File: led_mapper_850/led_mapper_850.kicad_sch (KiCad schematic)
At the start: 1082 parts, among them J1 Conn_02x12_Top_Bottom

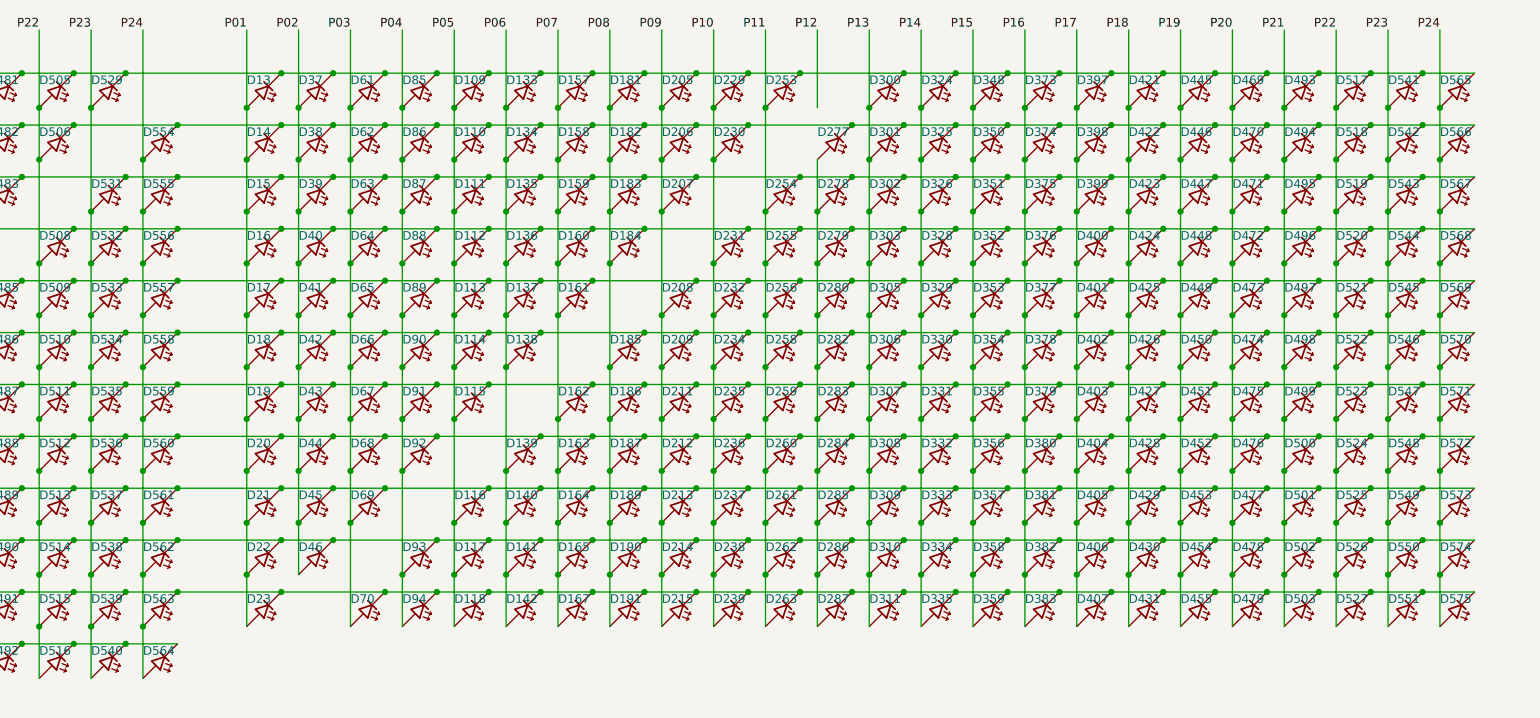
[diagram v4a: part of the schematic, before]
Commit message: fix horizontal connections
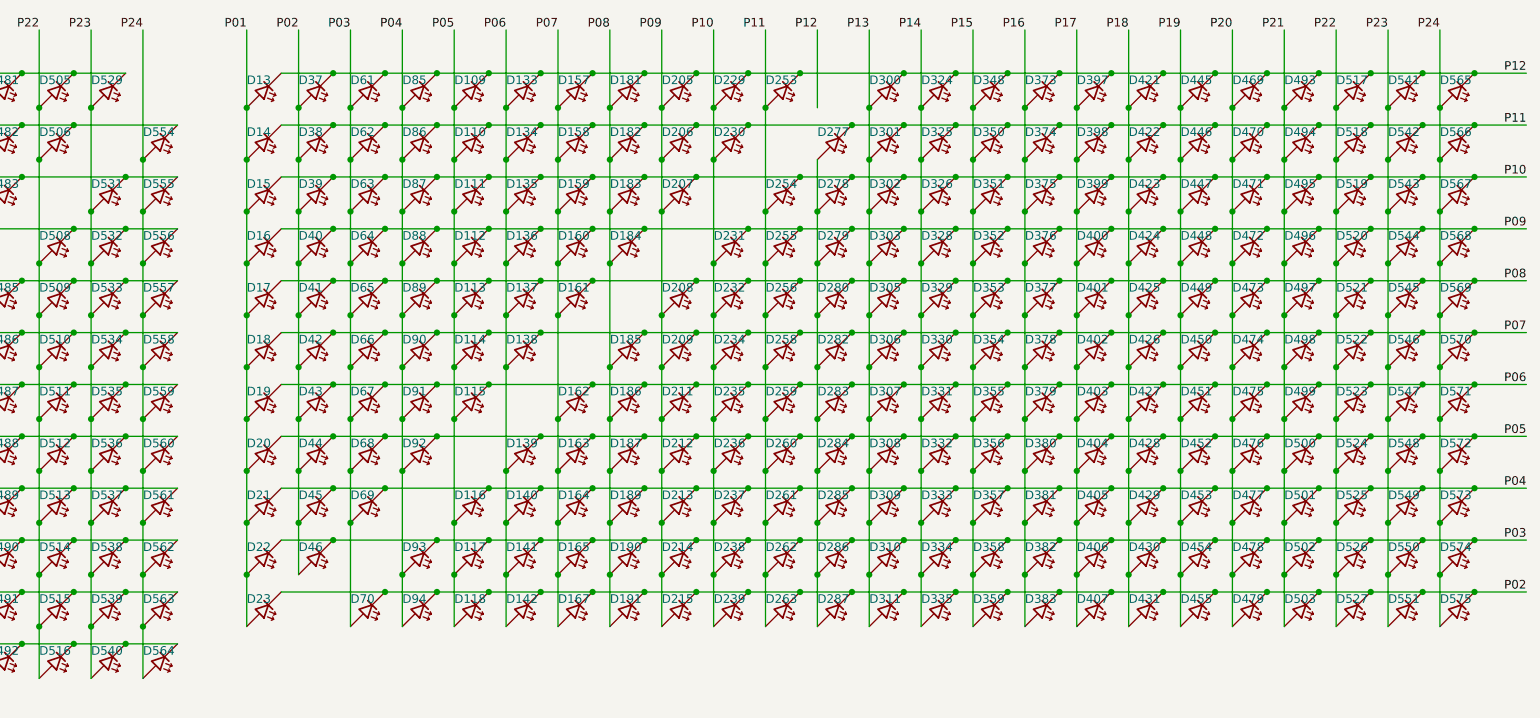
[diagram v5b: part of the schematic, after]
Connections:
- net P02: now also D118.1 (K), D142.1 (K), D167.1 (K), D191.1 (K), D215.1 (K), D23.1 (K), D239.1 (K), D263.1 (K), D287.1 (K), D311.1 (K), D335.1 (K), D359.1 (K), D383.1 (K), D407.1 (K), D431.1 (K), D455.1 (K), D479.1 (K), D503.1 (K), D527.1 (K), D551.1 (K), D575.1 (K), D70.1 (K), D94.1 (K)
- net P03: now also D117.1 (K), D141.1 (K), D165.1 (K), D190.1 (K), D214.1 (K), D22.1 (K), D238.1 (K), D262.1 (K), D286.1 (K), D310.1 (K), D334.1 (K), D358.1 (K), D382.1 (K), D406.1 (K), D430.1 (K), D454.1 (K), D46.1 (K), D478.1 (K), D502.1 (K), D526.1 (K), D550.1 (K), D574.1 (K), D93.1 (K)
- net P04: now also D116.1 (K), D140.1 (K), D164.1 (K), D189.1 (K), D21.1 (K), D213.1 (K), D237.1 (K), D261.1 (K), D285.1 (K), D309.1 (K), D333.1 (K), D357.1 (K), D381.1 (K), D405.1 (K), D429.1 (K), D45.1 (K), D453.1 (K), D477.1 (K), D501.1 (K), D525.1 (K), D549.1 (K), D573.1 (K), D69.1 (K)
- net P05: now also D139.1 (K), D163.1 (K), D187.1 (K), D20.1 (K), D212.1 (K), D236.1 (K), D260.1 (K), D284.1 (K), D308.1 (K), D332.1 (K), D356.1 (K), D380.1 (K), D404.1 (K), D428.1 (K), D44.1 (K), D452.1 (K), D476.1 (K), D500.1 (K), D524.1 (K), D548.1 (K), D572.1 (K), D68.1 (K), D92.1 (K)
- net P06: now also D115.1 (K), D162.1 (K), D186.1 (K), D19.1 (K), D211.1 (K), D235.1 (K), D259.1 (K), D283.1 (K), D307.1 (K), D331.1 (K), D355.1 (K), D379.1 (K), D403.1 (K), D427.1 (K), D43.1 (K), D451.1 (K), D475.1 (K), D499.1 (K), D523.1 (K), D547.1 (K), D571.1 (K), D67.1 (K), D91.1 (K)
- net P07: now also D114.1 (K), D138.1 (K), D18.1 (K), D185.1 (K), D209.1 (K), D234.1 (K), D258.1 (K), D282.1 (K), D306.1 (K), D330.1 (K), D354.1 (K), D378.1 (K), D402.1 (K), D42.1 (K), D426.1 (K), D450.1 (K), D474.1 (K), D498.1 (K), D522.1 (K), D546.1 (K), D570.1 (K), D66.1 (K), D90.1 (K)
- net P08: now also D113.1 (K), D137.1 (K), D161.1 (K), D17.1 (K), D208.1 (K), D232.1 (K), D256.1 (K), D280.1 (K), D305.1 (K), D329.1 (K), D353.1 (K), D377.1 (K), D401.1 (K), D41.1 (K), D425.1 (K), D449.1 (K), D473.1 (K), D497.1 (K), D521.1 (K), D545.1 (K), D569.1 (K), D65.1 (K), D89.1 (K)
- net P09: now also D112.1 (K), D136.1 (K), D16.1 (K), D160.1 (K), D184.1 (K), D231.1 (K), D255.1 (K), D279.1 (K), D303.1 (K), D328.1 (K), D352.1 (K), D376.1 (K), D40.1 (K), D400.1 (K), D424.1 (K), D448.1 (K), D472.1 (K), D496.1 (K), D520.1 (K), D544.1 (K), D568.1 (K), D64.1 (K), D88.1 (K)
- net P10: now also D111.1 (K), D135.1 (K), D15.1 (K), D159.1 (K), D183.1 (K), D207.1 (K), D254.1 (K), D278.1 (K), D302.1 (K), D326.1 (K), D351.1 (K), D375.1 (K), D39.1 (K), D399.1 (K), D423.1 (K), D447.1 (K), D471.1 (K), D495.1 (K), D519.1 (K), D543.1 (K), D567.1 (K), D63.1 (K), D87.1 (K)
- net P11: now also D110.1 (K), D134.1 (K), D14.1 (K), D158.1 (K), D182.1 (K), D206.1 (K), D230.1 (K), D277.1 (K), D301.1 (K), D325.1 (K), D350.1 (K), D374.1 (K), D38.1 (K), D398.1 (K), D422.1 (K), D446.1 (K), D470.1 (K), D494.1 (K), D518.1 (K), D542.1 (K), D566.1 (K), D62.1 (K), D86.1 (K)
- net P12: now also D109.1 (K), D13.1 (K), D133.1 (K), D157.1 (K), D181.1 (K), D205.1 (K), D229.1 (K), D253.1 (K), D300.1 (K), D324.1 (K), D348.1 (K), D37.1 (K), D373.1 (K), D397.1 (K), D421.1 (K), D445.1 (K), D469.1 (K), D493.1 (K), D517.1 (K), D541.1 (K), D565.1 (K), D61.1 (K), D85.1 (K)
- net P14: no longer D118.1 (K), D142.1 (K), D167.1 (K), D191.1 (K), D215.1 (K), D23.1 (K), D239.1 (K), D263.1 (K), D287.1 (K), D311.1 (K), D335.1 (K), D359.1 (K), D383.1 (K), D407.1 (K), D431.1 (K), D455.1 (K), D479.1 (K), D503.1 (K), D527.1 (K), D551.1 (K), D575.1 (K), D70.1 (K), D94.1 (K)
- net P15: no longer D117.1 (K), D141.1 (K), D165.1 (K), D190.1 (K), D214.1 (K), D22.1 (K), D238.1 (K), D262.1 (K), D286.1 (K), D310.1 (K), D334.1 (K), D358.1 (K), D382.1 (K), D406.1 (K), D430.1 (K), D454.1 (K), D46.1 (K), D478.1 (K), D502.1 (K), D526.1 (K), D550.1 (K), D574.1 (K), D93.1 (K)
- net P16: no longer D116.1 (K), D140.1 (K), D164.1 (K), D189.1 (K), D21.1 (K), D213.1 (K), D237.1 (K), D261.1 (K), D285.1 (K), D309.1 (K), D333.1 (K), D357.1 (K), D381.1 (K), D405.1 (K), D429.1 (K), D45.1 (K), D453.1 (K), D477.1 (K), D501.1 (K), D525.1 (K), D549.1 (K), D573.1 (K), D69.1 (K)
- net P17: no longer D139.1 (K), D163.1 (K), D187.1 (K), D20.1 (K), D212.1 (K), D236.1 (K), D260.1 (K), D284.1 (K), D308.1 (K), D332.1 (K), D356.1 (K), D380.1 (K), D404.1 (K), D428.1 (K), D44.1 (K), D452.1 (K), D476.1 (K), D500.1 (K), D524.1 (K), D548.1 (K), D572.1 (K), D68.1 (K), D92.1 (K)
- net P18: no longer D115.1 (K), D162.1 (K), D186.1 (K), D19.1 (K), D211.1 (K), D235.1 (K), D259.1 (K), D283.1 (K), D307.1 (K), D331.1 (K), D355.1 (K), D379.1 (K), D403.1 (K), D427.1 (K), D43.1 (K), D451.1 (K), D475.1 (K), D499.1 (K), D523.1 (K), D547.1 (K), D571.1 (K), D67.1 (K), D91.1 (K)
- net P19: no longer D114.1 (K), D138.1 (K), D18.1 (K), D185.1 (K), D209.1 (K), D234.1 (K), D258.1 (K), D282.1 (K), D306.1 (K), D330.1 (K), D354.1 (K), D378.1 (K), D402.1 (K), D42.1 (K), D426.1 (K), D450.1 (K), D474.1 (K), D498.1 (K), D522.1 (K), D546.1 (K), D570.1 (K), D66.1 (K), D90.1 (K)
- net P20: no longer D113.1 (K), D137.1 (K), D161.1 (K), D17.1 (K), D208.1 (K), D232.1 (K), D256.1 (K), D280.1 (K), D305.1 (K), D329.1 (K), D353.1 (K), D377.1 (K), D401.1 (K), D41.1 (K), D425.1 (K), D449.1 (K), D473.1 (K), D497.1 (K), D521.1 (K), D545.1 (K), D569.1 (K), D65.1 (K), D89.1 (K)
- net P22: no longer D111.1 (K), D135.1 (K), D15.1 (K), D159.1 (K), D183.1 (K), D207.1 (K), D254.1 (K), D278.1 (K), D302.1 (K), D326.1 (K), D351.1 (K), D375.1 (K), D39.1 (K), D399.1 (K), D423.1 (K), D447.1 (K), D471.1 (K), D495.1 (K), D519.1 (K), D543.1 (K), D567.1 (K), D63.1 (K), D87.1 (K)
- net P23: no longer D110.1 (K), D134.1 (K), D14.1 (K), D158.1 (K), D182.1 (K), D206.1 (K), D230.1 (K), D277.1 (K), D301.1 (K), D325.1 (K), D350.1 (K), D374.1 (K), D38.1 (K), D398.1 (K), D422.1 (K), D446.1 (K), D470.1 (K), D494.1 (K), D518.1 (K), D542.1 (K), D566.1 (K), D62.1 (K), D86.1 (K)
- net P24: no longer D109.1 (K), D13.1 (K), D133.1 (K), D157.1 (K), D181.1 (K), D205.1 (K), D229.1 (K), D253.1 (K), D300.1 (K), D324.1 (K), D348.1 (K), D37.1 (K), D373.1 (K), D397.1 (K), D421.1 (K), D445.1 (K), D469.1 (K), D493.1 (K), D517.1 (K), D541.1 (K), D565.1 (K), D61.1 (K), D85.1 (K)
- new net: D292.1 (K), D316.1 (K), D340.1 (K), D364.1 (K), D388.1 (K), D412.1 (K), D436.1 (K), D460.1 (K), D508.1 (K), D532.1 (K), D556.1 (K)

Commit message: remove old file
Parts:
- removed D1000, D1001, D1002, D1003, D1004, D1005, D1006, D1007, D1008, D1009, D1010, D1011, D1012, D1013, D1014, D1015, D1016, D1017, D1018, D1019, D1020, D1021, D1022, D1023, D1024, D1025, D1026, D1027, D1028, D1029, D1030, D1031, D1032, D1033, D1034, D1035, D1036, D1037, D1038, D1039, D1040, D1041, D1042, D1043, D1044, D1045, D1046, D1047, D1048, D1049, D1050, D1051, D1052, D1053, D1054, D1055, D1056, D1057, D1058, D1059, D1060, D1061, D1062, D1063, D1064, D1065, D1066, D1067, D1068, D1069, D1070, D1071, D1072, D1073, D1074, D1075, D1076, D1077, D1078, D1079, D1080, D1081, D1082, D1083, D1084, D1085, D1086, D1087, D1088, D1089, D1090, D1091, D1092, D1093, D1094, D1095, D1096, D1097, D1098, D1099, D1100, D1101, D1102, D1103, D1104, D119, D143, D166, D188, D210, D233, D257, D27, D281, D304, D327, D349, D372, D392, D416, D439, D461, D484, D50, D507, D530, D553, D577, D578, D579, D580, D581, D582, D583, D584, D585, D586, D587, D588, D589, D590, D591, D592, D593, D594, D595, D596, D597, D598, D599, D600, D601, D602, D603, D604, D605, D606, D607, D608, D609, D610, D611, D612, D613, D614, D615, D616, D617, D618, D619, D620, D621, D622, D623, D624, D625, D626, D627, D628, D629, D630, D631, D632, D633, D634, D635, D636, D637, D638, D639, D640, D641, D642, D643, D644, D645, D646, D647, D648, D649, D650, D651, D652, D653, D654, D655, D656, D657, D658, D659, D660, D661, D662, D663, D664, D665, D666, D667, D668, D669, D670, D671, D672, D673, D674, D675, D676, D677, D678, D679, D680, D681, D682, D683, D684, D685, D686, D687, D688, D689, D690, D691, D692, D693, D694, D695, D696, D697, D698, D699, D700, D701, D702, D703, D704, D705, D706, D707, D708, D709, D710, D711, D712, D713, D714, D715, D716, D717, D718, D719, D720, D721, D722, D723, D724, D725, D726, D727, D728, D729, D730, D731, D732, D733, D734, D735, D736, D737, D738, D739, D74, D740, D741, D742, D743, D744, D745, D746, D747, D748, D749, D750, D751, D752, D753, D754, D755, D756, D757, D758, D759, D760, D761, D762, D763, D764, D765, D766, D767, D768, D769, D770, D771, D772, D773, D774, D775, D776, D777, D778, D779, D780, D781, D782, D783, D784, D785, D786, D787, D788, D789, D790, D791, D792, D793, D794, D795, D796, D797, D798, D799, D800, D801, D802, D803, D804, D805, D806, D807, D808, D809, D810, D811, D812, D813, D814, D815, D816, D817, D818, D819, D820, D821, D822, D823, D824, D825, D826, D827, D828, D829, D830, D831, D832, D833, D834, D835, D836, D837, D838, D839, D840, D841, D842, D843, D844, D845, D846, D847, D848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: LED, LED_SMD:LED_0201_0603Metric, symbol Device:LED_45deg

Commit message: copy/flip/rotate shenanigans to organise refdes into rows
after diagonals are collapsed left-right (such that there are 12 rows), references are simply listed left to right then top to bottom
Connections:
- net P01: now also D100.2 (A), D125.2 (A), D150.2 (A), D175.2 (A), D200.2 (A), D225.2 (A), D24.2 (A), D250.2 (A), D275.2 (A), D300.2 (A), D325.2 (A), D351.2 (A)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; no longer D10.2 (A), D11.2 (A), D12.2 (A), D13.2 (A), D14.2 (A), D15.2 (A), D16.2 (A), D17.2 (A), D18.2 (A), D19.2 (A), D2.2 (A), D20.2 (A)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
- net P02: now also D101.2 (A), D126.2 (A), D151.2 (A), D176.2 (A), D2.2 (A), D201.2 (A), D226.2 (A), D251.2 (A), D276.2 (A), D301.2 (A), D326.2 (A), D352.2 (A)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; no longer D118.1 (K), D142.1 (K), D167.1 (K), D191.1 (K), D215.1 (K), D23.1 (K), D239.1 (K), D24.2 (A), D26.2 (A), D263.1 (K), D28.2 (A), D287.1 (K)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
- net P03: now also D102.2 (A), D127.2 (A), D152.2 (A), D177.2 (A), D202.2 (A), D227.2 (A), D252.2 (A), D26.2 (A), D277.2 (A), D3.2 (A), D302.2 (A), D328.2 (A)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; no longer D117.1 (K), D141.1 (K), D165.1 (K), D190.1 (K), D214.1 (K), D22.1 (K), D238.1 (K), D262.1 (K), D286.1 (K), D310.1 (K), D334.1 (K), D358.1 (K)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
- net P04: now also D103.2 (A), D128.2 (A), D153.2 (A), D178.2 (A), D203.2 (A), D228.2 (A), D253.2 (A), D278.2 (A), D28.2 (A), D303.2 (A), D329.2 (A), D354.2 (A)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; no longer D116.1 (K), D140.1 (K), D164.1 (K), D189.1 (K), D21.1 (K), D213.1 (K), D237.1 (K), D261.1 (K), D285.1 (K), D309.1 (K), D333.1 (K), D357.1 (K)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
- net P05: now also D129.2 (A), D154.2 (A), D179.2 (A), D204.2 (A), D229.2 (A), D254.2 (A), D279.2 (A), D29.2 (A), D305.2 (A), D330.2 (A), D355.2 (A), D376.1 (K)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; no longer D100.2 (A), D101.2 (A), D102.2 (A), D103.2 (A), D105.2 (A), D106.2 (A), D107.2 (A), D108.2 (A), D109.2 (A), D110.2 (A), D111.2 (A), D112.2 (A)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
- net P06: now also D105.2 (A), D155.2 (A), D180.2 (A), D205.2 (A), D230.2 (A), D255.2 (A), D280.2 (A), D30.2 (A), D306.2 (A), D325.1 (K), D326.1 (K), D328.1 (K)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; no longer D115.1 (K), D121.2 (A), D122.2 (A), D123.2 (A), D124.2 (A), D125.2 (A), D126.2 (A), D127.2 (A), D128.2 (A), D129.2 (A), D131.2 (A), D132.2 (A)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
- net P07: now also D106.2 (A), D131.2 (A), D181.2 (A), D206.2 (A), D231.2 (A), D256.2 (A), D275.1 (K), D276.1 (K), D277.1 (K), D278.1 (K), D279.1 (K), D280.1 (K)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; no longer D114.1 (K), D138.1 (K), D145.2 (A), D146.2 (A), D147.2 (A), D148.2 (A), D149.2 (A), D150.2 (A), D151.2 (A), D152.2 (A), D153.2 (A), D154.2 (A)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
- net P08: now also D107.2 (A), D132.2 (A), D157.2 (A), D207.2 (A), D225.1 (K), D226.1 (K), D227.1 (K), D228.1 (K), D229.1 (K), D230.1 (K), D231.1 (K), D234.1 (K)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; no longer D113.1 (K), D137.1 (K), D161.1 (K), D169.2 (A), D17.1 (K), D170.2 (A), D171.2 (A), D172.2 (A), D173.2 (A), D174.2 (A), D175.2 (A), D176.2 (A)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
- net P09: now also D108.2 (A), D133.2 (A), D158.2 (A), D175.1 (K), D176.1 (K), D177.1 (K), D178.1 (K), D179.1 (K), D180.1 (K), D181.1 (K), D182.1 (K), D183.1 (K)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; no longer D112.1 (K), D136.1 (K), D16.1 (K), D160.1 (K), D193.2 (A), D194.2 (A), D195.2 (A), D196.2 (A), D197.2 (A), D198.2 (A), D199.2 (A), D200.2 (A)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
- net P10: now also D10.2 (A), D109.2 (A), D125.1 (K), D126.1 (K), D127.1 (K), D128.1 (K), D129.1 (K), D130.1 (K), D131.1 (K), D132.1 (K), D133.1 (K), D134.1 (K)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; no longer D111.1 (K), D15.1 (K), D159.1 (K), D183.1 (K), D207.1 (K), D217.2 (A), D218.2 (A), D219.2 (A), D220.2 (A), D221.2 (A), D222.2 (A), D223.2 (A)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
- net P11: now also D11.2 (A), D110.2 (A), D134.2 (A), D160.2 (A), D184.2 (A), D211.2 (A), D235.2 (A), D285.2 (A), D311.2 (A), D335.2 (A), D35.2 (A), D362.2 (A)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; no longer D110.1 (K), D134.1 (K), D14.1 (K), D158.1 (K), D182.1 (K), D206.1 (K), D230.1 (K), D241.2 (A), D242.2 (A), D243.2 (A), D244.2 (A), D245.2 (A)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
- net P12: now also D111.2 (A), D12.2 (A), D161.2 (A), D212.2 (A), D24.1 (K), D25.1 (K), D26.1 (K), D262.2 (A), D28.1 (K), D29.1 (K), D30.1 (K), D31.1 (K)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; no longer D109.1 (K), D13.1 (K), D133.1 (K), D157.1 (K), D181.1 (K), D205.1 (K), D229.1 (K), D253.1 (K), D265.2 (A), D266.2 (A), D267.2 (A), D268.2 (A)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
- net P13: now also D112.2 (A), D13.2 (A), D136.2 (A), D162.2 (A), D186.2 (A), D213.2 (A), D237.2 (A), D263.2 (A), D287.2 (A), D314.2 (A), D338.2 (A), D36.2 (A)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; no longer D108.1 (K), D12.1 (K), D132.1 (K), D156.1 (K), D180.1 (K), D204.1 (K), D228.1 (K), D252.1 (K), D276.1 (K), D289.2 (A), D290.2 (A), D291.2 (A)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
- net P14: now also D113.2 (A), D137.2 (A), D14.2 (A), D163.2 (A), D187.2 (A), D214.2 (A), D238.2 (A), D265.2 (A), D289.2 (A), D339.2 (A), D365.2 (A), D37.2 (A)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; no longer D107.1 (K), D11.1 (K), D131.1 (K), D155.1 (K), D179.1 (K), D203.1 (K), D227.1 (K), D251.1 (K), D275.1 (K), D299.1 (K), D313.2 (A), D314.2 (A)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
- net P15: now also D114.2 (A), D138.2 (A), D15.2 (A), D164.2 (A), D189.2 (A), D215.2 (A), D239.2 (A), D266.2 (A), D290.2 (A), D316.2 (A), D366.2 (A), D38.2 (A)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; no longer D10.1 (K), D106.1 (K), D130.1 (K), D154.1 (K), D178.1 (K), D202.1 (K), D226.1 (K), D250.1 (K), D274.1 (K), D298.1 (K), D322.1 (K), D337.2 (A)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
- net P16: now also D115.2 (A), D139.2 (A), D16.2 (A), D165.2 (A), D190.2 (A), D217.2 (A), D241.2 (A), D267.2 (A), D291.2 (A), D317.2 (A), D341.2 (A), D39.2 (A)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; no longer D105.1 (K), D129.1 (K), D153.1 (K), D177.1 (K), D201.1 (K), D225.1 (K), D249.1 (K), D273.1 (K), D297.1 (K), D321.1 (K), D33.1 (K), D345.1 (K)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
- net P17: now also D116.2 (A), D140.2 (A), D167.2 (A), D17.2 (A), D191.2 (A), D218.2 (A), D242.2 (A), D268.2 (A), D292.2 (A), D318.2 (A), D342.2 (A), D351.1 (K)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; no longer D104.1 (K), D128.1 (K), D152.1 (K), D176.1 (K), D200.1 (K), D224.1 (K), D248.1 (K), D272.1 (K), D296.1 (K), D32.1 (K), D320.1 (K), D344.1 (K)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
- net P18: now also D117.2 (A), D141.2 (A), D169.2 (A), D18.2 (A), D193.2 (A), D219.2 (A), D243.2 (A), D269.2 (A), D293.2 (A), D300.1 (K), D301.1 (K), D302.1 (K)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; no longer D103.1 (K), D127.1 (K), D151.1 (K), D175.1 (K), D199.1 (K), D223.1 (K), D247.1 (K), D271.1 (K), D295.1 (K), D31.1 (K), D343.1 (K), D367.1 (K)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
- net P19: now also D118.2 (A), D142.2 (A), D170.2 (A), D19.2 (A), D194.2 (A), D220.2 (A), D244.2 (A), D250.1 (K), D251.1 (K), D252.1 (K), D253.1 (K), D254.1 (K)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; no longer D102.1 (K), D126.1 (K), D150.1 (K), D174.1 (K), D198.1 (K), D222.1 (K), D246.1 (K), D294.1 (K), D30.1 (K), D318.1 (K), D342.1 (K), D366.1 (K)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
- net P20: now also D121.2 (A), D145.2 (A), D171.2 (A), D195.2 (A), D20.2 (A), D200.1 (K), D201.1 (K), D202.1 (K), D203.1 (K), D204.1 (K), D205.1 (K), D206.1 (K)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; no longer D101.1 (K), D125.1 (K), D149.1 (K), D173.1 (K), D197.1 (K), D245.1 (K), D269.1 (K), D29.1 (K), D293.1 (K), D317.1 (K), D341.1 (K), D365.1 (K)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
- net P21: now also D122.2 (A), D146.2 (A), D150.1 (K), D151.1 (K), D152.1 (K), D153.1 (K), D154.1 (K), D155.1 (K), D156.1 (K), D157.1 (K), D158.1 (K), D159.1 (K)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; no longer D100.1 (K), D124.1 (K), D148.1 (K), D172.1 (K), D196.1 (K), D220.1 (K), D244.1 (K), D268.1 (K), D28.1 (K), D4.1 (K), D481.2 (A), D482.2 (A)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
- net P22: now also D100.1 (K), D101.1 (K), D102.1 (K), D103.1 (K), D104.1 (K), D105.1 (K), D106.1 (K), D107.1 (K), D108.1 (K), D109.1 (K), D110.1 (K), D111.1 (K)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; no longer D147.1 (K), D171.1 (K), D195.1 (K), D219.1 (K), D243.1 (K), D26.1 (K), D267.1 (K), D291.1 (K), D3.1 (K), D315.1 (K), D339.1 (K), D363.1 (K)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
- net P23: now also D123.2 (A), D148.2 (A), D173.2 (A), D198.2 (A), D223.2 (A), D23.2 (A), D248.2 (A), D273.2 (A), D298.2 (A), D323.2 (A), D348.2 (A), D374.2 (A)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; no longer D122.1 (K), D146.1 (K), D170.1 (K), D194.1 (K), D2.1 (K), D218.1 (K), D242.1 (K), D25.1 (K), D266.1 (K), D290.1 (K), D314.1 (K), D338.1 (K)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
- net P24: now also D10.1 (K), D11.1 (K), D12.1 (K), D124.2 (A), D13.1 (K), D14.1 (K), D149.2 (A), D15.1 (K), D16.1 (K), D17.1 (K), D174.2 (A), D18.1 (K)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; no longer D121.1 (K), D145.1 (K), D169.1 (K), D193.1 (K), D217.1 (K), D24.1 (K), D241.1 (K), D265.1 (K), D289.1 (K), D313.1 (K), D337.1 (K), D361.1 (K)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
- new net: D135.2 (A), D185.2 (A), D236.2 (A), D286.2 (A), D337.2 (A), D387.2 (A), D437.2 (A), D488.2 (A), D538.2 (A), D85.2 (A)
- new net: D162.1 (K), D163.1 (K), D164.1 (K), D165.1 (K), D167.1 (K), D169.1 (K), D170.1 (K), D171.1 (K), D172.1 (K), D173.1 (K), D174.1 (K)

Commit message: fix missing wire & references
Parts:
- removed D531, D532, D533, D534, D535, D536, D537, D538, D539, D540, D541, D542, D543, D544, D545, D546, D547, D548, D549, D550, D551, D554, D555, D556, D557, D558, D559, D560, D561, D562, D563, D564, D565, D566, D567, D568, D569, D570, D571, D572, D573, D574, D575: LED, LED_SMD:LED_0201_0603Metric, symbol Device:LED_45deg
- added D119, D120, D143, D144, D166, D168, D188, D192, D210, D216, D233, D240, D257, D264, D27, D281, D288, D304, D312, D327, D336, D349, D360, D372, D384, D392, D408, D416, D432, D439, D456, D461, D47, D480, D484, D50, D504, D507, D528, D71, D74, D95, D97: LED, LED_SMD:LED_0201_0603Metric, symbol Device:LED_45deg
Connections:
- net P01: now also D116.2 (A), D139.2 (A), D162.2 (A), D185.2 (A), D208.2 (A), D231.2 (A), D254.2 (A), D277.2 (A), D323.2 (A), D346.2 (A), D369.2 (A), D415.2 (A)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; no longer D100.2 (A), D125.2 (A), D150.2 (A), D175.2 (A), D200.2 (A), D225.2 (A), D250.2 (A), D275.2 (A), D325.2 (A), D351.2 (A), D376.2 (A), D401.2 (A)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
- net P02: now also D117.2 (A), D140.2 (A), D163.2 (A), D186.2 (A), D209.2 (A), D232.2 (A), D255.2 (A), D278.2 (A), D324.2 (A), D347.2 (A), D370.2 (A), D393.2 (A)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; no longer D101.2 (A), D126.2 (A), D151.2 (A), D176.2 (A), D201.2 (A), D226.2 (A), D251.2 (A), D276.2 (A), D326.2 (A), D352.2 (A), D377.2 (A), D402.2 (A)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
- net P03: now also D118.2 (A), D141.2 (A), D164.2 (A), D187.2 (A), D256.2 (A), D279.2 (A), D325.2 (A), D348.2 (A), D371.2 (A), D394.2 (A), D417.2 (A), D438.1 (K)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; no longer D102.2 (A), D127.2 (A), D152.2 (A), D177.2 (A), D202.2 (A), D227.2 (A), D252.2 (A), D277.2 (A), D328.2 (A), D353.2 (A), D378.2 (A), D403.2 (A)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
- net P04: now also D142.2 (A), D165.2 (A), D211.2 (A), D234.2 (A), D280.2 (A), D326.2 (A), D393.1 (K), D394.1 (K), D395.1 (K), D396.1 (K), D397.1 (K), D398.1 (K)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; no longer D103.2 (A), D128.2 (A), D153.2 (A), D178.2 (A), D203.2 (A), D228.2 (A), D253.2 (A), D278.2 (A), D28.2 (A), D329.2 (A), D354.2 (A), D379.2 (A)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
- net P05: now also D189.2 (A), D212.2 (A), D235.2 (A), D258.2 (A), D28.2 (A), D346.1 (K), D347.1 (K), D348.1 (K), D350.1 (K), D351.1 (K), D352.1 (K), D353.1 (K)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; no longer D104.2 (A), D129.2 (A), D154.2 (A), D179.2 (A), D204.2 (A), D229.2 (A), D254.2 (A), D279.2 (A), D29.2 (A), D305.2 (A), D330.2 (A), D355.2 (A)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
- net P06: now also D121.2 (A), D167.2 (A), D190.2 (A), D213.2 (A), D236.2 (A), D259.2 (A), D282.2 (A), D29.2 (A), D300.1 (K), D301.1 (K), D302.1 (K), D303.1 (K)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; no longer D105.2 (A), D130.2 (A), D155.2 (A), D180.2 (A), D205.2 (A), D230.2 (A), D255.2 (A), D280.2 (A), D30.2 (A), D306.2 (A), D325.1 (K), D326.1 (K)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
- net P07: now also D122.2 (A), D145.2 (A), D191.2 (A), D214.2 (A), D237.2 (A), D254.1 (K), D255.1 (K), D256.1 (K), D258.1 (K), D259.1 (K), D260.1 (K), D261.1 (K)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; no longer D106.2 (A), D131.2 (A), D156.2 (A), D181.2 (A), D206.2 (A), D231.2 (A), D256.2 (A), D277.1 (K), D278.1 (K), D279.1 (K), D280.1 (K), D282.1 (K)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
- net P08: now also D100.2 (A), D123.2 (A), D146.2 (A), D169.2 (A), D208.1 (K), D209.1 (K), D211.1 (K), D212.1 (K), D213.1 (K), D214.1 (K), D215.1 (K), D217.1 (K)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; no longer D107.2 (A), D132.2 (A), D157.2 (A), D182.2 (A), D207.2 (A), D231.1 (K), D232.1 (K), D234.1 (K), D235.1 (K), D236.1 (K), D237.1 (K), D238.1 (K)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
- net P09: now also D101.2 (A), D124.2 (A), D147.2 (A), D162.1 (K), D163.1 (K), D164.1 (K), D165.1 (K), D167.1 (K), D169.1 (K), D170.1 (K), D171.1 (K), D172.1 (K)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; no longer D108.2 (A), D133.2 (A), D158.2 (A), D185.1 (K), D186.1 (K), D187.1 (K), D189.1 (K), D190.1 (K), D191.1 (K), D193.1 (K), D194.1 (K), D195.1 (K)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
- net P10: now also D102.2 (A), D116.1 (K), D117.1 (K), D118.1 (K), D121.1 (K), D122.1 (K), D123.1 (K), D124.1 (K), D148.2 (A), D170.2 (A), D194.2 (A), D262.2 (A)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; no longer D109.2 (A), D139.1 (K), D140.1 (K), D141.1 (K), D142.1 (K), D145.1 (K), D146.1 (K), D147.1 (K), D148.1 (K), D149.1 (K), D159.2 (A), D183.2 (A)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
- net P11: now also D103.2 (A), D125.2 (A), D149.2 (A), D171.2 (A), D195.2 (A), D217.2 (A), D241.2 (A), D263.2 (A), D287.2 (A), D309.2 (A), D333.2 (A), D34.2 (A)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; no longer D110.2 (A), D134.2 (A), D160.2 (A), D184.2 (A), D211.2 (A), D235.2 (A), D261.2 (A), D285.2 (A), D311.2 (A), D335.2 (A), D35.2 (A), D362.2 (A)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
- net P12: now also D104.2 (A), D126.2 (A), D150.2 (A), D172.2 (A), D196.2 (A), D218.2 (A), D242.2 (A), D310.2 (A), D334.2 (A), D356.2 (A), D380.2 (A), D402.2 (A)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; no longer D111.2 (A), D161.2 (A), D212.2 (A), D262.2 (A), D313.2 (A), D363.2 (A), D413.2 (A), D464.2 (A), D48.1 (K), D514.2 (A), D61.2 (A)
- net P13: now also D105.2 (A), D127.2 (A), D151.2 (A), D173.2 (A), D197.2 (A), D219.2 (A), D243.2 (A), D265.2 (A), D289.2 (A), D311.2 (A), D335.2 (A), D35.2 (A)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; no longer D112.2 (A), D136.2 (A), D162.2 (A), D186.2 (A), D213.2 (A), D237.2 (A), D263.2 (A), D287.2 (A), D314.2 (A), D338.2 (A), D36.2 (A), D364.2 (A)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
- net P14: now also D106.2 (A), D128.2 (A), D152.2 (A), D174.2 (A), D198.2 (A), D220.2 (A), D244.2 (A), D266.2 (A), D290.2 (A), D358.2 (A), D36.2 (A), D382.2 (A)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; no longer D113.2 (A), D137.2 (A), D163.2 (A), D187.2 (A), D214.2 (A), D238.2 (A), D265.2 (A), D289.2 (A), D315.2 (A), D339.2 (A), D365.2 (A), D37.2 (A)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
- net P15: now also D107.2 (A), D129.2 (A), D153.2 (A), D175.2 (A), D199.2 (A), D221.2 (A), D245.2 (A), D267.2 (A), D291.2 (A), D313.2 (A), D337.2 (A), D359.2 (A)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; no longer D114.2 (A), D138.2 (A), D164.2 (A), D189.2 (A), D215.2 (A), D239.2 (A), D266.2 (A), D290.2 (A), D316.2 (A), D340.2 (A), D366.2 (A), D38.2 (A)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
- net P16: now also D108.2 (A), D130.2 (A), D154.2 (A), D176.2 (A), D200.2 (A), D222.2 (A), D246.2 (A), D268.2 (A), D292.2 (A), D314.2 (A), D338.2 (A), D369.1 (K)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; no longer D115.2 (A), D139.2 (A), D165.2 (A), D190.2 (A), D217.2 (A), D241.2 (A), D267.2 (A), D291.2 (A), D317.2 (A), D341.2 (A), D367.2 (A), D39.2 (A)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
- net P17: now also D109.2 (A), D131.2 (A), D155.2 (A), D177.2 (A), D201.2 (A), D223.2 (A), D247.2 (A), D269.2 (A), D293.2 (A), D315.2 (A), D323.1 (K), D324.1 (K)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; no longer D116.2 (A), D140.2 (A), D167.2 (A), D191.2 (A), D218.2 (A), D242.2 (A), D268.2 (A), D292.2 (A), D318.2 (A), D342.2 (A), D351.1 (K), D352.1 (K)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
- net P18: now also D110.2 (A), D132.2 (A), D156.2 (A), D178.2 (A), D202.2 (A), D224.2 (A), D248.2 (A), D270.2 (A), D277.1 (K), D278.1 (K), D279.1 (K), D280.1 (K)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; no longer D117.2 (A), D141.2 (A), D169.2 (A), D193.2 (A), D219.2 (A), D243.2 (A), D269.2 (A), D293.2 (A), D300.1 (K), D301.1 (K), D302.1 (K), D303.1 (K)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
- net P19: now also D111.2 (A), D133.2 (A), D157.2 (A), D179.2 (A), D203.2 (A), D225.2 (A), D231.1 (K), D232.1 (K), D234.1 (K), D235.1 (K), D236.1 (K), D237.1 (K)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; no longer D118.2 (A), D142.2 (A), D170.2 (A), D194.2 (A), D220.2 (A), D244.2 (A), D254.1 (K), D255.1 (K), D256.1 (K), D258.1 (K), D259.1 (K), D260.1 (K)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
- net P20: now also D112.2 (A), D134.2 (A), D158.2 (A), D180.2 (A), D185.1 (K), D186.1 (K), D187.1 (K), D189.1 (K), D190.1 (K), D191.1 (K), D193.1 (K), D194.1 (K)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; no longer D121.2 (A), D145.2 (A), D171.2 (A), D195.2 (A), D208.1 (K), D209.1 (K), D211.1 (K), D212.1 (K), D213.1 (K), D214.1 (K), D215.1 (K), D217.1 (K)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
- net P21: now also D113.2 (A), D135.2 (A), D139.1 (K), D140.1 (K), D141.1 (K), D142.1 (K), D145.1 (K), D146.1 (K), D147.1 (K), D148.1 (K), D149.1 (K), D181.2 (A)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; no longer D122.2 (A), D146.2 (A), D151.1 (K), D152.1 (K), D153.1 (K), D154.1 (K), D155.1 (K), D156.1 (K), D157.1 (K), D158.1 (K), D159.1 (K), D160.1 (K)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
- net P22: now also D136.2 (A), D159.2 (A), D182.2 (A), D205.2 (A), D228.2 (A), D251.2 (A), D274.2 (A), D320.2 (A), D343.2 (A), D366.2 (A), D389.2 (A), D412.2 (A)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; no longer D116.1 (K), D117.1 (K), D118.1 (K), D121.1 (K), D122.1 (K), D123.1 (K), D124.1 (K), D147.2 (A), D172.2 (A), D197.2 (A), D222.2 (A), D247.2 (A)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
- net P23: now also D114.2 (A), D137.2 (A), D160.2 (A), D183.2 (A), D206.2 (A), D229.2 (A), D252.2 (A), D275.2 (A), D321.2 (A), D344.2 (A), D367.2 (A), D390.2 (A)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; no longer D123.2 (A), D148.2 (A), D173.2 (A), D198.2 (A), D223.2 (A), D248.2 (A), D273.2 (A), D323.2 (A), D348.2 (A), D374.2 (A), D399.2 (A), D424.2 (A)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
- net P24: now also D115.2 (A), D138.2 (A), D161.2 (A), D184.2 (A), D207.2 (A), D230.2 (A), D253.2 (A), D276.2 (A), D322.2 (A), D345.2 (A), D368.2 (A), D391.2 (A)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; no longer D124.2 (A), D149.2 (A), D174.2 (A), D199.2 (A), D224.2 (A), D249.2 (A), D274.2 (A), D324.2 (A), D350.2 (A), D375.2 (A), D400.2 (A), D425.2 (A)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
- new net: D151.1 (K), D152.1 (K), D153.1 (K), D154.1 (K), D155.1 (K), D156.1 (K), D157.1 (K), D158.1 (K), D159.1 (K), D160.1 (K), D161.1 (K)
